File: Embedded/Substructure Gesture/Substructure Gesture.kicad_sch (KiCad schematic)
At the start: 2 parts, among them J1 VL53L0X

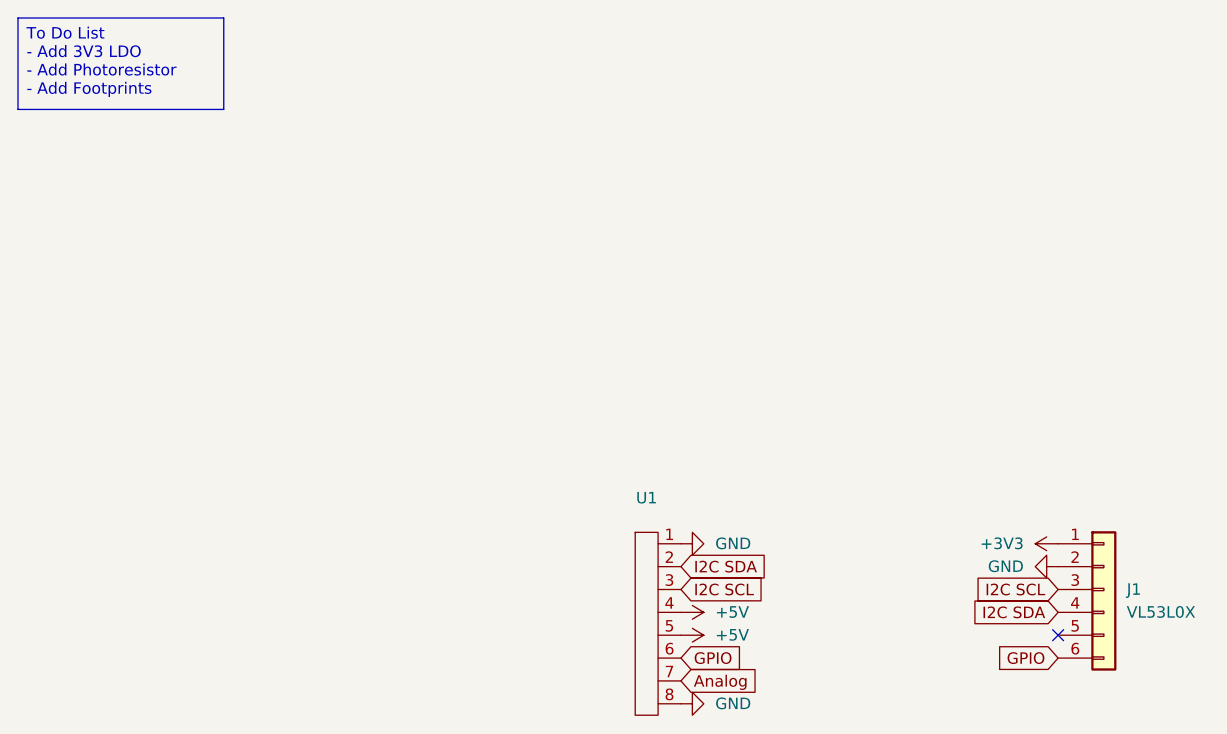
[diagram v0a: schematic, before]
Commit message: Added Footprints, Photoresistor & LDO
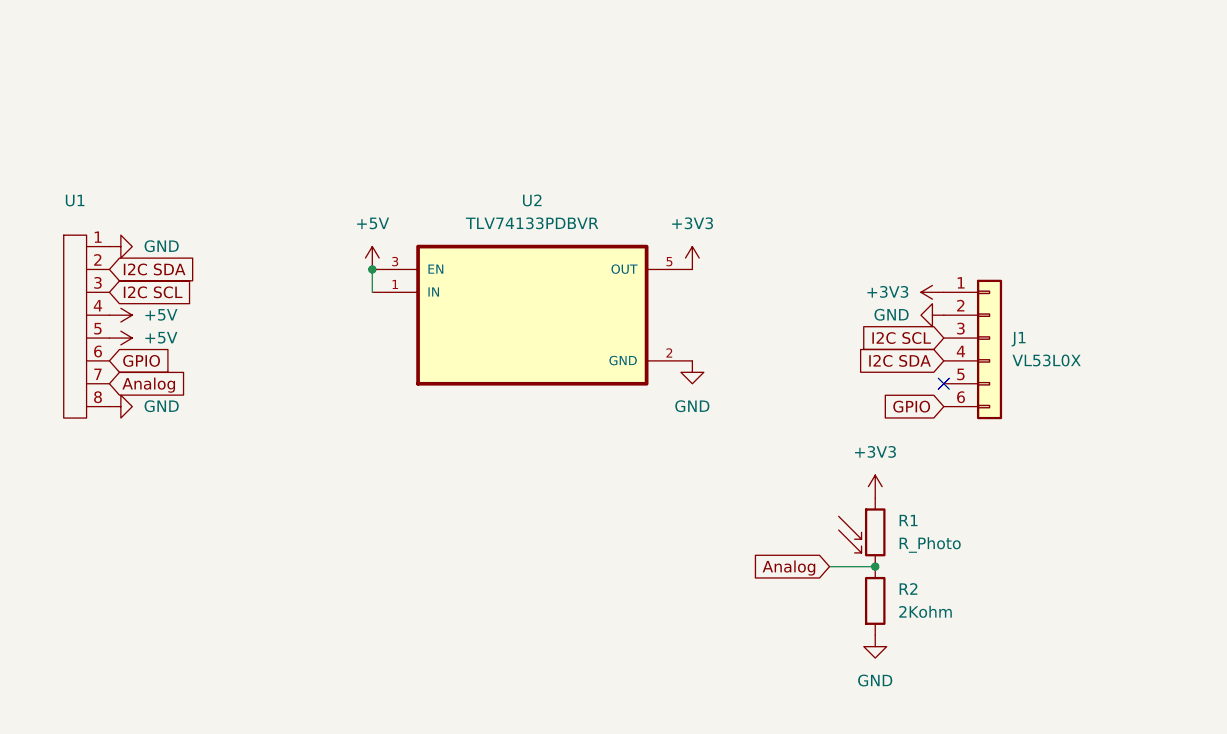
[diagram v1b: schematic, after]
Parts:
- added R1: R_Photo, OptoDevice:R_LDR_5.1x4.3mm_P3.4mm_Vertical, symbol Device:R_Photo
- added R2: 2Kohm, Resistor_SMD:R_0603_1608Metric_Pad0.98x0.95mm_HandSolder, symbol Device:R
- added U2: TLV74133PDBVR, TLV 3V3 Regulator:SOT95P280X145-5N, symbol TLV 3V3 Regulator:TLV74133PDBVR
- J1: footprint (none) -> Connector_PinHeader_2.54mm:PinHeader_1x06_P2.54mm_Vertical
- U1: footprint (none) -> FFC:FFC 0.8mm 8P
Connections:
- net +3V3: now also R1.1, U2.5 (OUT)
- net +5V: now also U2.1 (IN), U2.3 (EN)
- net Analog: now also R1.2, R2.1
- net GND: now also R2.2, U2.2 (GND)
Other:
- moved on the sheet: J1, U1
